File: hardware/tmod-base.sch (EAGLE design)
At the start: 97 parts, among them IC1 TPS70933, IC10 TPS70933, IC2 INA219SOT, IC3 STM32L052C8T6, IC4 HX1, IC5 LMP7702, IC6 TPS62143, IC8 TPS22918, IC9 BME280, J1 DNP, J2 GPS1, J3 TEMP, J4 POWER, J5 GPS2, J6 MICRO-SD_CARD_SOCKET, J7 HAB-EXP, U2 ADXL345, Y1 8M, Y2 32768

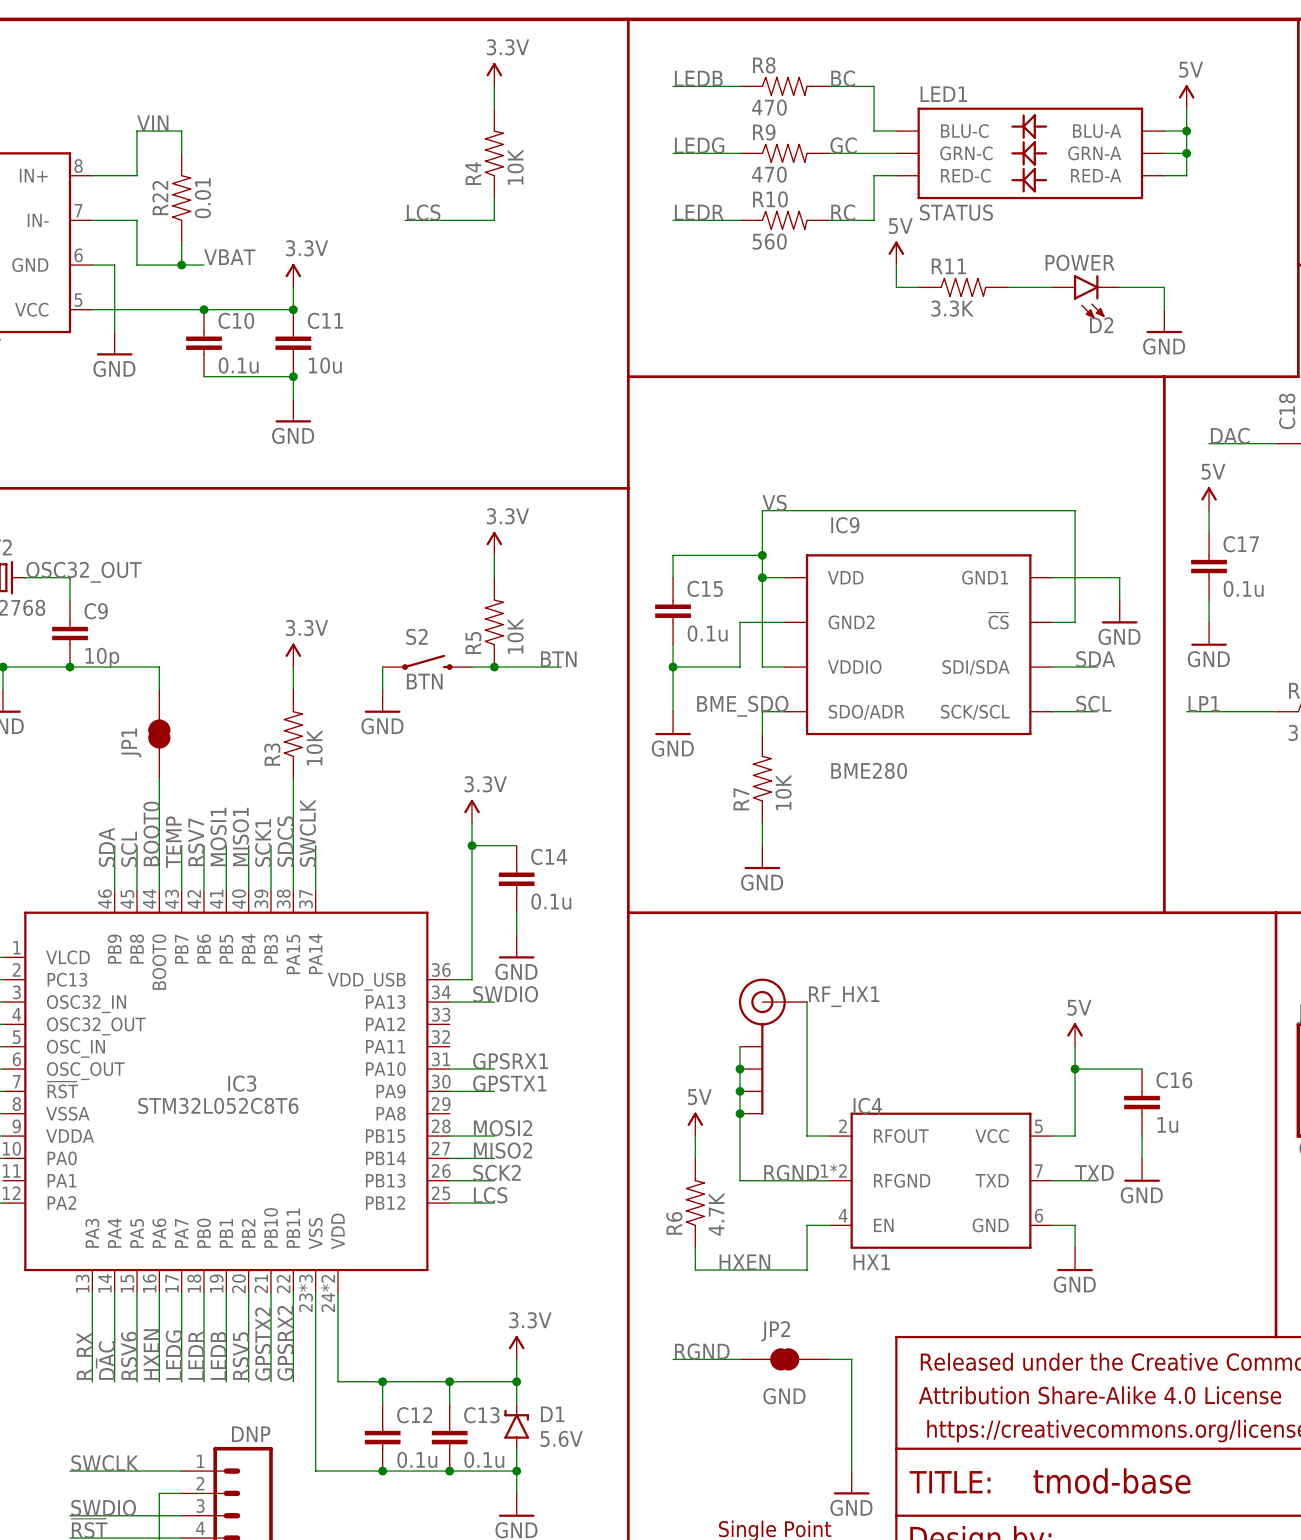
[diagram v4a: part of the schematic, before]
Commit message: Rotate LED by 180 degrees to match the actual part
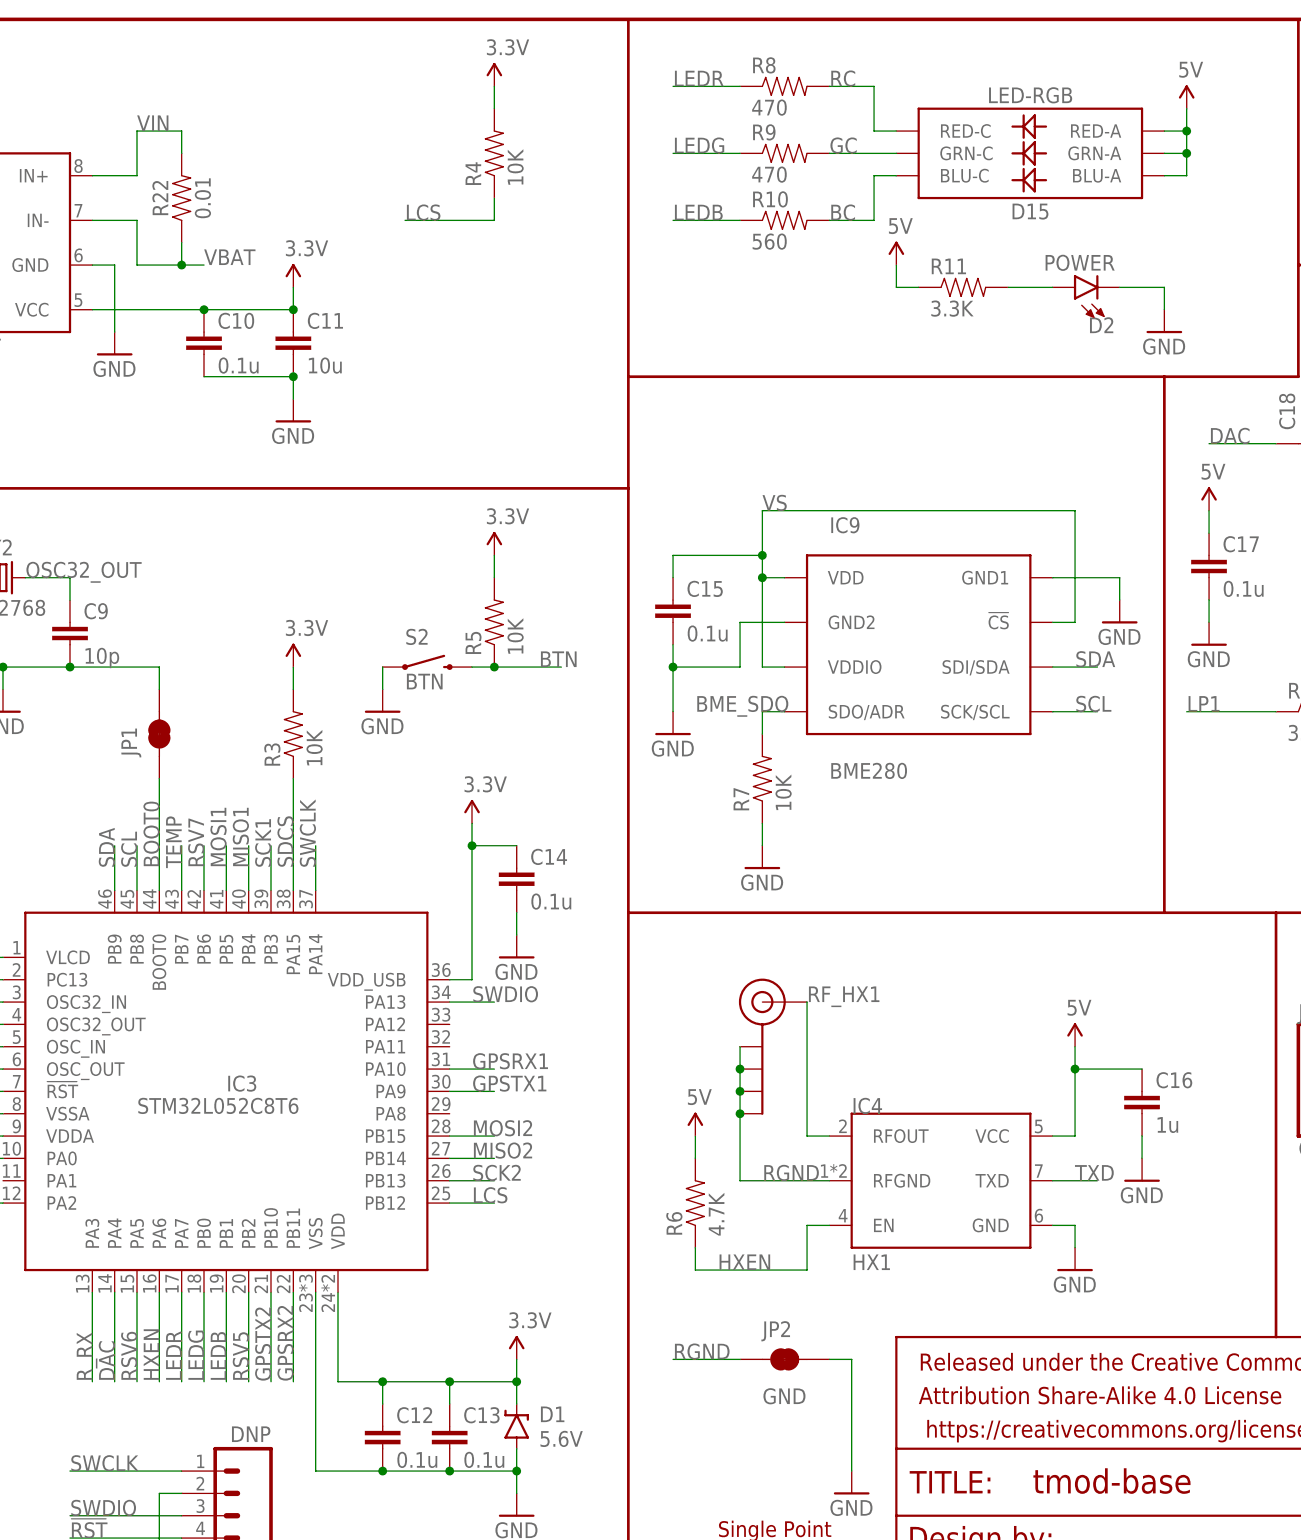
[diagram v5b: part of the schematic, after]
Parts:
- removed LED1: STATUS, SparkFun-LED:LED-TRICOLOR-5050NO_IC
- added D15: LED-RGB, HAB:LED-RGB
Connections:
- net 5V: now also D15.BLU-A, D15.GRN-A, D15.RED-A; no longer LED1.BLU-A, LED1.GRN-A, LED1.RED-A
- net BC: now also D15.BLU-C, R10.2; no longer LED1.BLU-C, R8.2
- net GC: now also D15.GRN-C; no longer LED1.GRN-C
- net LEDB: now also R10.1; no longer R8.1
- net LEDG: now also IC3.PB0; no longer IC3.PA7
- net LEDR: now also IC3.PA7, R8.1; no longer IC3.PB0, R10.1
- net RC: now also D15.RED-C, R8.2; no longer LED1.RED-C, R10.2
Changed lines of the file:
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@@
 <part name="GND32" library="SparkFun-Aesthetics" deviceset="GND" device=""/>
 <part name="R20" library="SparkFun-Passives" deviceset="RESISTOR" device="0805-RES" value="10K"/>
-<part name="LED1" library="SparkFun-LED" deviceset="LED-TRICOLOR-5050" device="NO_IC" value="STATUS"/>
 <part name="SUPPLY15" library="SparkFun-Aesthetics" deviceset="5V" device=""/>
 <part name="R8" library="SparkFun-Passives" deviceset="RESISTOR" device="0805-RES" value="470"/>
@@
 <part name="D14" library="SparkFun-DiscreteSemi" deviceset="DIODE-ZENER" device="5.6V" value="5.6V"/>
 <part name="GND46" library="SparkFun-Aesthetics" deviceset="GND" device=""/>
+<part name="D15" library="HAB" deviceset="LED-RGB" device=""/>
 </parts>
 <sheets>
@@
 <instance part="GND32" gate="1" x="322.58" y="99.06"/>
 <instance part="R20" gate="G$1" x="322.58" y="111.76" rot="R90"/>
-<instance part="LED1" gate="D1" x="162.56" y="170.18"/>
 <instance part="SUPPLY15" gate="G$1" x="180.34" y="175.26"/>
 <instance part="R8" gate="G$1" x="134.62" y="177.8"/>
@@
 </instance>
 <instance part="GND46" gate="1" x="459.74" y="111.76"/>
+<instance part="D15" gate="G$1" x="162.56" y="170.18" rot="R180"/>
 </instances>
 <busses>
@@
 <pinref part="SUPPLY15" gate="G$1" pin="5V"/>
 <wire x1="180.34" y1="175.26" x2="180.34" y2="172.72" width="0.1524" layer="91"/>
-<pinref part="LED1" gate="D1" pin="BLU-A"/>
 <wire x1="180.34" y1="172.72" x2="177.8" y2="172.72" width="0.1524" layer="91"/>
 <wire x1="180.34" y1="172.72" x2="180.34" y2="170.18" width="0.1524" layer="91"/>
 <junction x="180.34" y="172.72"/>
-<pinref part="LED1" gate="D1" pin="GRN-A"/>
 <wire x1="180.34" y1="170.18" x2="177.8" y2="170.18" width="0.1524" layer="91"/>
-<pinref part="LED1" gate="D1" pin="RED-A"/>
 <wire x1="177.8" y1="167.64" x2="180.34" y2="167.64" width="0.1524" layer="91"/>
 <wire x1="180.34" y1="167.64" x2="180.34" y2="170.18" width="0.1524" layer="91"/>
 <junction x="180.34" y="170.18"/>
+<pinref part="D15" gate="G$1" pin="BLU-A"/>
+<pinref part="D15" gate="G$1" pin="GRN-A"/>
+<pinref part="D15" gate="G$1" pin="RED-A"/>
 </segment>
 <segment>
@@
 </segment>
 </net>
-<net name="RC" class="0">
+<net name="GC" class="0">
+<segment>
+<pinref part="R9" gate="G$1" pin="2"/>
+<wire x1="139.7" y1="170.18" x2="147.32" y2="170.18" width="0.1524" layer="91"/>
+<label x="139.7" y="170.18" size="1.778" layer="95"/>
+<pinref part="D15" gate="G$1" pin="GRN-C"/>
+</segment>
+</net>
+<net name="BC" class="0">
 <segment>
 <pinref part="R10" gate="G$1" pin="2"/>
 <wire x1="139.7" y1="162.56" x2="144.78" y2="162.56" width="0.1524" layer="91"/>
 <wire x1="144.78" y1="162.56" x2="144.78" y2="167.64" width="0.1524" layer="91"/>
-<pinref part="LED1" gate="D1" pin="RED-C"/>
 <wire x1="144.78" y1="167.64" x2="147.32" y2="167.64" width="0.1524" layer="91"/>
 <label x="139.7" y="162.56" size="1.778" layer="95"/>
-</segment>
-</net>
-<net name="GC" class="0">
-<segment>
-<pinref part="R9" gate="G$1" pin="2"/>
-<pinref part="LED1" gate="D1" pin="GRN-C"/>
-<wire x1="139.7" y1="170.18" x2="147.32" y2="170.18" width="0.1524" layer="91"/>
-<label x="139.7" y="170.18" size="1.778" layer="95"/>
-</segment>
-</net>
-<net name="BC" class="0">
-<segment>
-<pinref part="LED1" gate="D1" pin="BLU-C"/>
-<wire x1="147.32" y1="172.72" x2="144.78" y2="172.72" width="0.1524" layer="91"/>
-<wire x1="144.78" y1="172.72" x2="144.78" y2="177.8" width="0.1524" layer="91"/>
-<pinref part="R8" gate="G$1" pin="2"/>
-<wire x1="144.78" y1="177.8" x2="139.7" y2="177.8" width="0.1524" layer="91"/>
-<label x="139.7" y="177.8" size="1.778" layer="95"/>
+<pinref part="D15" gate="G$1" pin="BLU-C"/>
 </segment>
 </net>
 <net name="LEDB" class="0">
+<segment>
+<pinref part="R10" gate="G$1" pin="1"/>
+<wire x1="121.92" y1="162.56" x2="129.54" y2="162.56" width="0.1524" layer="91"/>
+<label x="121.92" y="162.56" size="1.778" layer="95"/>
+</segment>
+<segment>
+<pinref part="IC3" gate="G$1" pin="PB1"/>
+<wire x1="71.12" y1="30.48" x2="71.12" y2="40.64" width="0.1524" layer="91"/>
+<label x="71.12" y="30.48" size="1.778" layer="95" rot="R90"/>
+</segment>
+</net>
+<net name="LEDG" class="0">
+<segment>
+<pinref part="R9" gate="G$1" pin="1"/>
+<wire x1="121.92" y1="170.18" x2="129.54" y2="170.18" width="0.1524" layer="91"/>
+<label x="121.92" y="170.18" size="1.778" layer="95"/>
+</segment>
+<segment>
+<pinref part="IC3" gate="G$1" pin="PB0"/>
+<wire x1="68.58" y1="30.48" x2="68.58" y2="40.64" width="0.1524" layer="91"/>
+<label x="68.58" y="30.48" size="1.778" layer="95" rot="R90"/>
+</segment>
+</net>
+<net name="LEDR" class="0">
 <segment>
 <pinref part="R8" gate="G$1" pin="1"/>
@@
 </segment>
 <segment>
-<pinref part="IC3" gate="G$1" pin="PB1"/>
-<wire x1="71.12" y1="30.48" x2="71.12" y2="40.64" width="0.1524" layer="91"/>
-<label x="71.12" y="30.48" size="1.778" layer="95" rot="R90"/>
-</segment>
-</net>
-<net name="LEDG" class="0">
-<segment>
-<pinref part="R9" gate="G$1" pin="1"/>
-<wire x1="121.92" y1="170.18" x2="129.54" y2="170.18" width="0.1524" layer="91"/>
-<label x="121.92" y="170.18" size="1.778" layer="95"/>
-</segment>
-<segment>
 <pinref part="IC3" gate="G$1" pin="PA7"/>
 <wire x1="66.04" y1="30.48" x2="66.04" y2="40.64" width="0.1524" layer="91"/>
 <label x="66.04" y="30.48" size="1.778" layer="95" rot="R90"/>
-</segment>
-</net>
-<net name="LEDR" class="0">
-<segment>
-<pinref part="R10" gate="G$1" pin="1"/>
-<wire x1="121.92" y1="162.56" x2="129.54" y2="162.56" width="0.1524" layer="91"/>
-<label x="121.92" y="162.56" size="1.778" layer="95"/>
-</segment>
-<segment>
-<pinref part="IC3" gate="G$1" pin="PB0"/>
-<wire x1="68.58" y1="30.48" x2="68.58" y2="40.64" width="0.1524" layer="91"/>
-<label x="68.58" y="30.48" size="1.778" layer="95" rot="R90"/>
 </segment>
 </net>
@@
 </segment>
 </net>
+<net name="RC" class="0">
+<segment>
+<wire x1="147.32" y1="172.72" x2="144.78" y2="172.72" width="0.1524" layer="91"/>
+<wire x1="144.78" y1="172.72" x2="144.78" y2="177.8" width="0.1524" layer="91"/>
+<pinref part="R8" gate="G$1" pin="2"/>
+<wire x1="144.78" y1="177.8" x2="139.7" y2="177.8" width="0.1524" layer="91"/>
+<label x="139.7" y="177.8" size="1.778" layer="95"/>
+<pinref part="D15" gate="G$1" pin="RED-C"/>
+</segment>
+</net>
